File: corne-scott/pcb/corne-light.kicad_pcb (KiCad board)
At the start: 2 copper layers, 271.8 x 105.6 mm, 118 parts, among them J1 MJ-4PP-9, J2 OLED, J5 Breakaway_Tabs, J6 MJ-4PP-9, J7 OLED, SW1 SW_PUSH, SW10 SW_PUSH, SW11 SW_PUSH, SW12 SW_PUSH, SW13 SW_PUSH, SW14 SW_PUSH, SW15 SW_PUSH, SW16 SW_PUSH, SW17 SW_PUSH, SW18 SW_PUSH, SW19 SW_PUSH, SW2 SW_PUSH, SW20 SW_PUSH, SW21 SW_PUSH, SW22 SW_PUSH, SW23 SW_PUSH, SW24 SW_PUSH, SW25 SW_PUSH, SW26 SW_PUSH, SW27 SW_PUSH, SW28 SW_PUSH, SW29 SW_PUSH, SW3 SW_PUSH, SW30 SW_PUSH, SW31 SW_PUSH, SW32 SW_PUSH, SW33 SW_PUSH, SW34 SW_PUSH, SW35 SW_PUSH, SW36 SW_PUSH, SW37 SW_PUSH, SW38 SW_PUSH, SW39 SW_PUSH, SW4 SW_PUSH, SW40 SW_PUSH, SW41 SW_PUSH, SW42 SW_PUSH, SW5 SW_PUSH, SW6 SW_PUSH, SW7 SW_PUSH, SW8 SW_PUSH, SW9 SW_PUSH, U1 ProMicro, U2 ProMicro

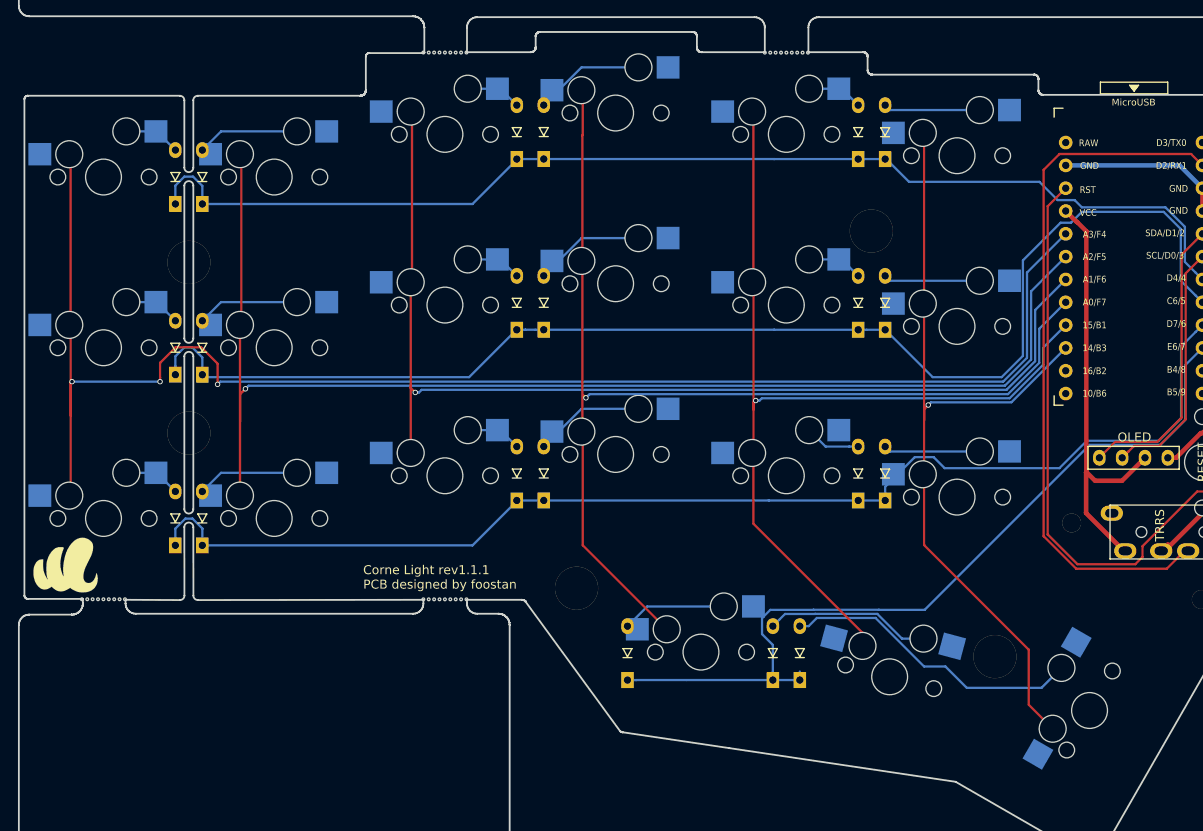
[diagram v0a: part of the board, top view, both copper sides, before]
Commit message: Rotate left side switches and diodes
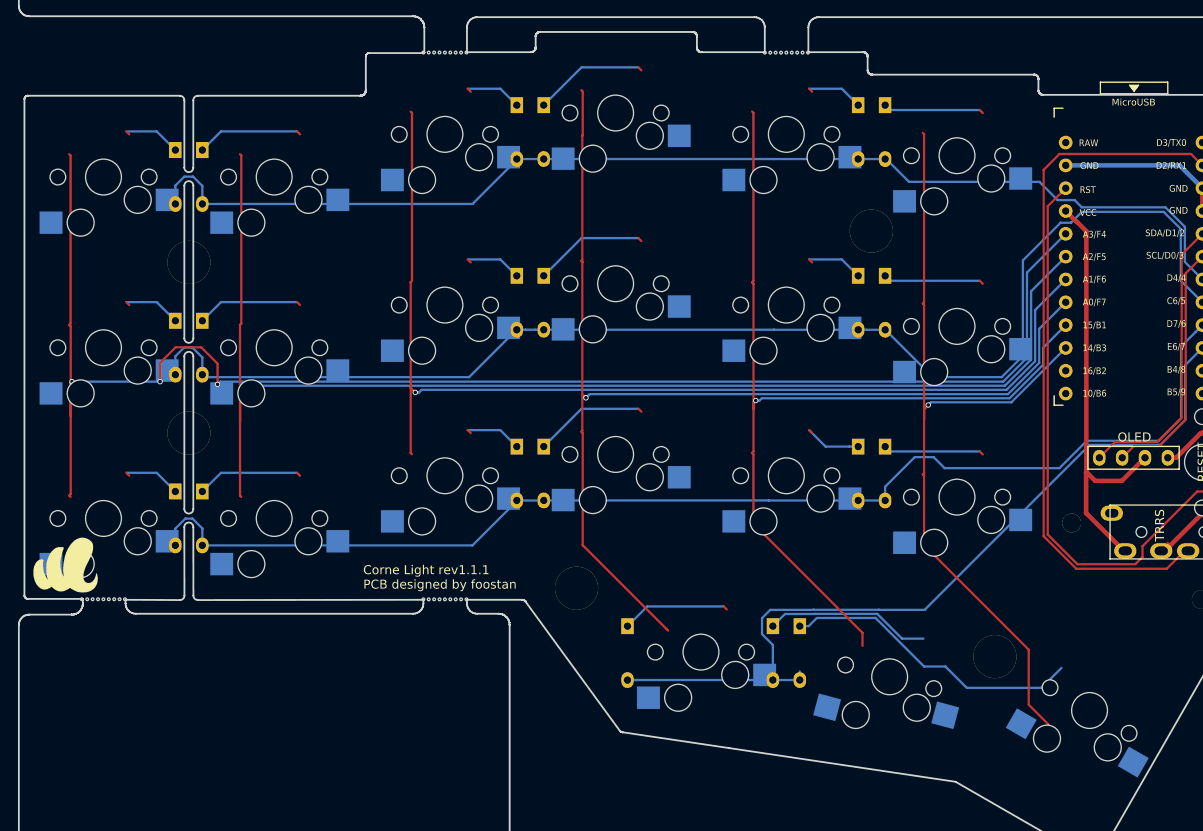
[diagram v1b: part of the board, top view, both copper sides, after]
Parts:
- D1, D10, D11, D12, D13, D14, D15, D16, D17, D18, D19, D2, D20, D21, D3, D4, D5, D6, D7, D8, D9: moved to B.Cu
- turned D1 to 270 degrees
- turned D10 to 270 degrees
- turned D11 to 270 degrees
- turned D12 to 270 degrees
- turned D13 to 270 degrees
- turned D14 to 270 degrees
- turned D15 to 270 degrees
- turned D16 to 270 degrees
- turned D17 to 270 degrees
- turned D18 to 270 degrees
- turned D19 to 270 degrees
- turned D2 to 270 degrees
- turned D20 to 270 degrees
- turned D21 to 270 degrees
- turned D3 to 270 degrees
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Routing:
- net row3: track 92.6 -> 156.3 mm
- net row2: track 135.8 -> 189.0 mm
- net row1: track 145.0 -> 198.2 mm
- net row0: track 129.2 -> 182.4 mm
- net Net-(D21-Pad2): track 33.6 -> 0.00 mm
- net Net-(D20-Pad2): track 18.5 -> 0.00 mm
- net Net-(D16-Pad2): track 12.3 -> 0.00 mm
- net Net-(D4-Pad2): track 12.3 -> 0.00 mm
- net Net-(D10-Pad2): track 12.3 -> 0.00 mm
- net Net-(D19-Pad2): track 11.6 -> 0.00 mm
- net Net-(D8-Pad2): track 11.4 -> 0.00 mm
- net Net-(D2-Pad2): track 11.4 -> 0.00 mm
- net Net-(D14-Pad2): track 11.4 -> 0.00 mm
- net Net-(D6-Pad2): track 10.8 -> 0.00 mm
- net Net-(D18-Pad2): track 10.8 -> 0.00 mm
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
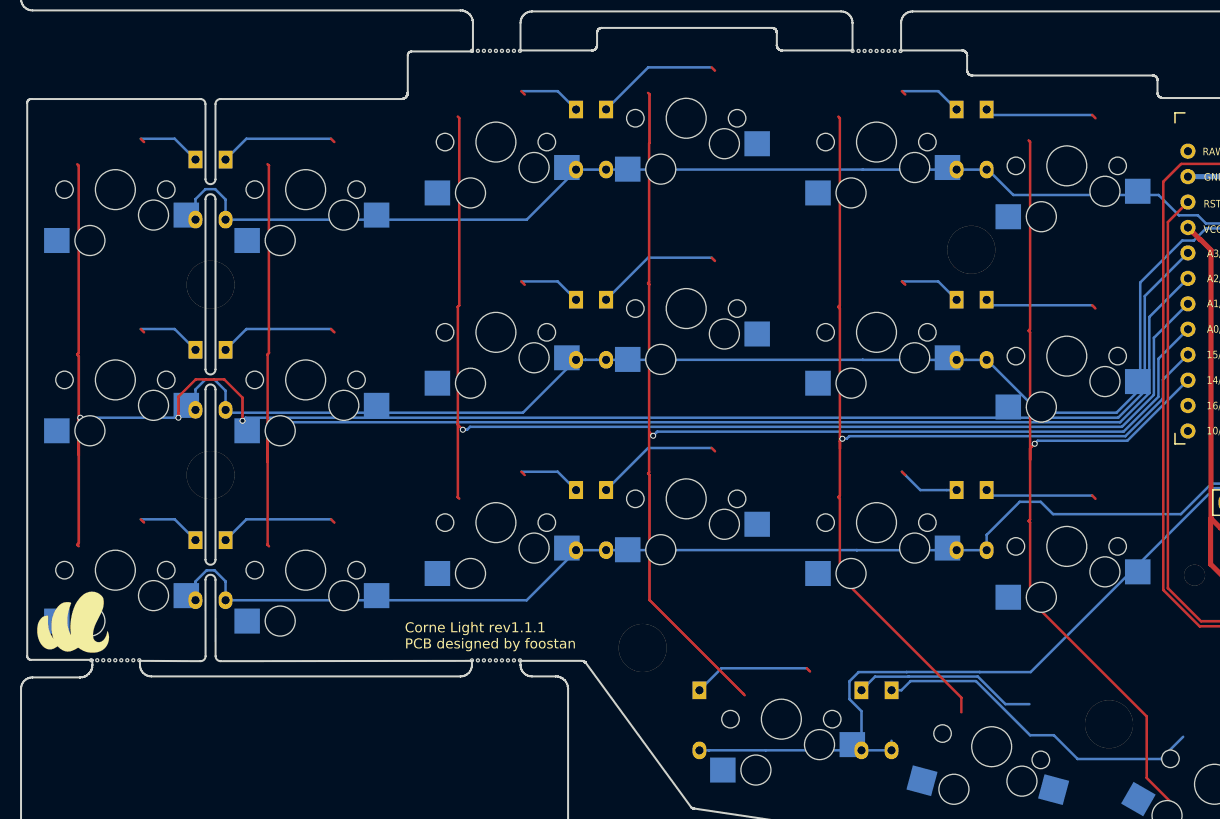
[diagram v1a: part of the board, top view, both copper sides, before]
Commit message: Adjust left side diodes
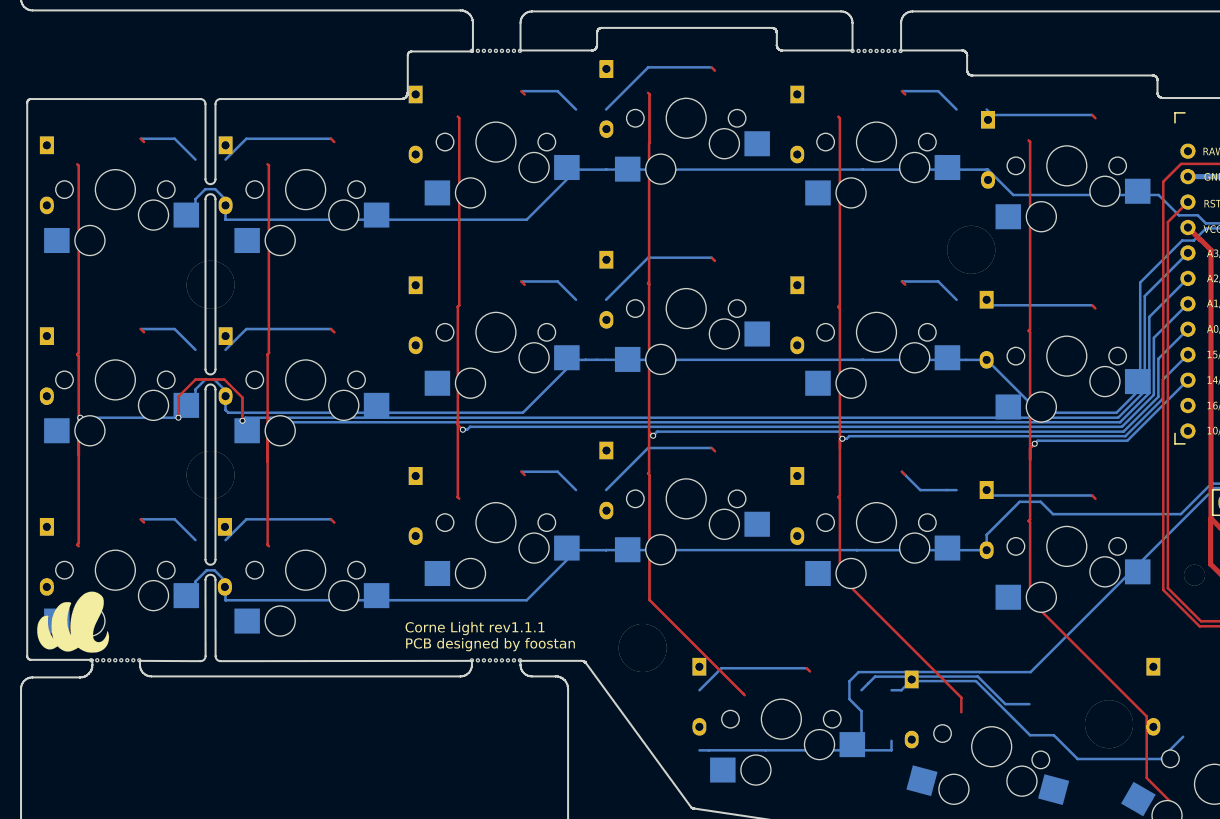
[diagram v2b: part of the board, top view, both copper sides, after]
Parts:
- moved D21 26.3 mm to (125.8, 96.6)
- moved D3 16.1 mm to (52.2, 39.4)
- moved D9 16.1 mm to (52.2, 58.5)
- moved D15 16.1 mm to (52.2, 77.5)
- moved D5 16.0 mm to (90.3, 39.4)
- moved D11 16.0 mm to (90.3, 58.5)
- moved D17 16.0 mm to (90.3, 77.5)
- moved D1 14.9 mm to (15.3, 44.5)
- moved D7 14.9 mm to (15.3, 63.5)
- moved D13 14.9 mm to (15.3, 82.6)
- moved D20 5.13 mm to (101.7, 97.8)
- moved D4 4.04 mm to (71.2, 36.9)
- moved D10 3.99 mm to (71.2, 55.9)
- moved D16 3.94 mm to (71.2, 75.0)
- moved D19 2.35 mm to (80.5, 96.6)
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
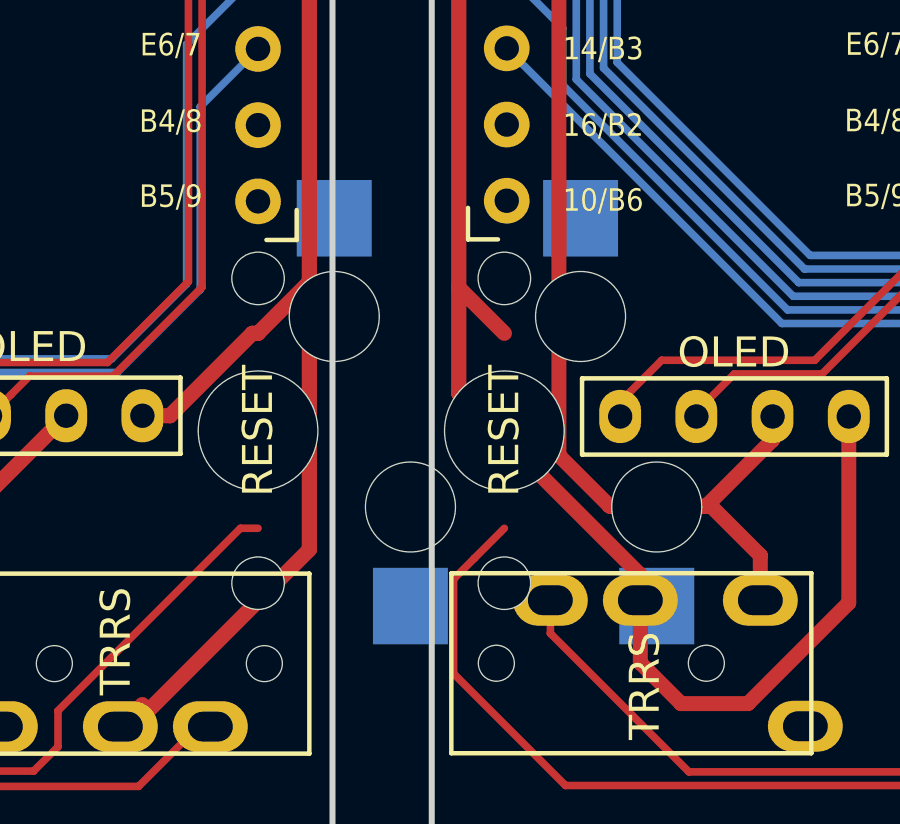
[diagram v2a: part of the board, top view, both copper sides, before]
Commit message: Add back reset switches I accidentally turned into mx switches
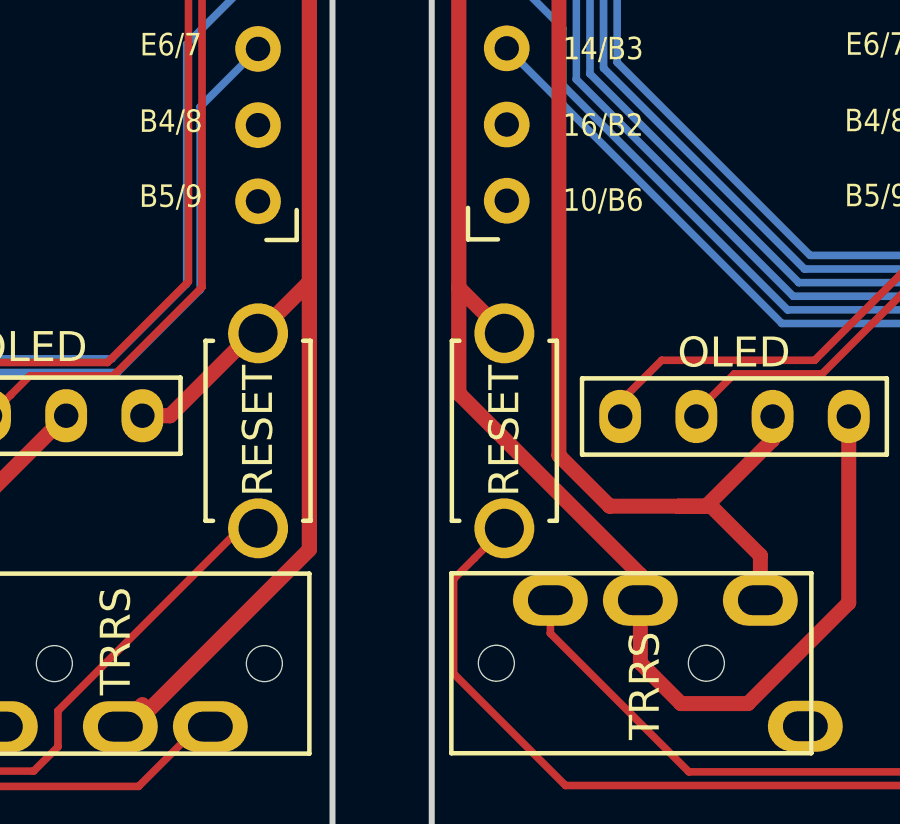
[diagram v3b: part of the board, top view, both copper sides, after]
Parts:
- RSW1, RSW2: footprint MX_Only:MXOnly-1U-Hotswap -> kbd:ResetSW_1side
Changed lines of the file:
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@@
     (add_net row3_r)
+  )
+  (module kbd:ResetSW_1side (layer F.Cu)
+    (at 152.7145 77.671 270)
+    (fp_text reference RSW2 (at 0 2.55 90) (layer F.SilkS) hide
+      (effects (font (size 1 1) (thickness 0.15)))
+    )
+    (fp_text value SW_PUSH (at 0 -2.55 90) (layer F.Fab)
+      (effects (font (size 1 1) (thickness 0.15)))
+    )
+    (fp_text user RESET (at 0 0 90) (layer F.SilkS)
+      (effects (font (size 1 1) (thickness 0.15)))
+    )
+    (fp_line (start 3 -1.75) (end 3 -1.5) (layer F.SilkS) (width 0.15))
+    (fp_line (start -3 -1.75) (end 3 -1.75) (layer F.SilkS) (width 0.15))
+    (fp_line (start -3 -1.75) (end -3 -1.5) (layer F.SilkS) (width 0.15))
+    (fp_line (start -3 1.75) (end -3 1.5) (layer F.SilkS) (width 0.15))
+    (fp_line (start 3 1.75) (end 3 1.5) (layer F.SilkS) (width 0.15))
+    (fp_line (start -3 1.75) (end 3 1.75) (layer F.SilkS) (width 0.15))
+    (fp_text user %R (at 0 3.048 90) (layer B.SilkS)
+      (effects (font (size 1 1) (thickness 0.15)) (justify mirror))
+    )
+    (pad 2 thru_hole circle (at -3.25 0 270) (size 2 2) (drill 1.3) (layers *.Cu F.SilkS B.Mask)
+      (net 88 GNDA))
+    (pad 1 thru_hole circle (at 3.25 0 270) (size 2 2) (drill 1.3) (layers *.Cu F.SilkS B.Mask)
+      (net 75 reset_r))
+  )
+  (module kbd:ResetSW_1side (layer F.Cu)
+    (at 144.5045 77.671 270)
+    (fp_text reference RSW1 (at 0 2.55 270) (layer F.SilkS) hide
+      (effects (font (size 1 1) (thickness 0.15)))
+    )
+    (fp_text value SW_PUSH (at 0 -2.55 270) (layer F.Fab)
+      (effects (font (size 1 1) (thickness 0.15)))
+    )
+    (fp_text user RESET (at 0 0 270) (layer F.SilkS)
+      (effects (font (size 1 1) (thickness 0.15)))
+    )
+    (fp_line (start 3 -1.75) (end 3 -1.5) (layer F.SilkS) (width 0.15))
+    (fp_line (start -3 -1.75) (end 3 -1.75) (layer F.SilkS) (width 0.15))
+    (fp_line (start -3 -1.75) (end -3 -1.5) (layer F.SilkS) (width 0.15))
+    (fp_line (start -3 1.75) (end -3 1.5) (layer F.SilkS) (width 0.15))
+    (fp_line (start 3 1.75) (end 3 1.5) (layer F.SilkS) (width 0.15))
+    (fp_line (start -3 1.75) (end 3 1.75) (layer F.SilkS) (width 0.15))
+    (fp_text user %R (at 0 3.048 90) (layer B.SilkS)
+      (effects (font (size 1 1) (thickness 0.15)) (justify mirror))
+    )
+    (pad 2 thru_hole circle (at -3.25 0 270) (size 2 2) (drill 1.3) (layers *.Cu F.SilkS B.Mask)
+      (net 26 GND))
+    (pad 1 thru_hole circle (at 3.25 0 270) (size 2 2) (drill 1.3) (layers *.Cu F.SilkS B.Mask)
+      (net 36 reset))
   )
   (module MX_Only:MXOnly-1U-Hotswap (layer F.Cu)
@@
     (pad "" np_thru_hole circle (at 2.54 -5.08 180) (size 3 3) (drill 3) (layers *.Cu *.Mask))
   )
-  (module MX_Only:MXOnly-1U-Hotswap (layer F.Cu)
-    (at 152.7145 77.671 270)
-    (attr smd)
-    (fp_text reference RSW2 (at 0 2.55 90) (layer F.SilkS) hide
-      (effects (font (size 1 1) (thickness 0.15)))
-    )
-    (fp_text value SW_PUSH (at 0 -2.55 90) (layer F.Fab)
-      (effects (font (size 1 1) (thickness 0.15)))
-    )
-    (fp_line (start -5.842 -1.27) (end -5.842 -3.81) (layer B.CrtYd) (width 0.15))
-    (fp_line (start -8.382 -1.27) (end -5.842 -1.27) (layer B.CrtYd) (width 0.15))
-    (fp_line (start -8.382 -3.81) (end -8.382 -1.27) (layer B.CrtYd) (width 0.15))
-    (fp_line (start -5.842 -3.81) (end -8.382 -3.81) (layer B.CrtYd) (width 0.15))
-    (fp_line (start 4.572 -3.81) (end 4.572 -6.35) (layer B.CrtYd) (width 0.15))
-    (fp_line (start 7.112 -3.81) (end 4.572 -3.81) (layer B.CrtYd) (width 0.15))
-    (fp_line (start 7.112 -6.35) (end 7.112 -3.81) (layer B.CrtYd) (width 0.15))
-    (fp_line (start 4.572 -6.35) (end 7.112 -6.35) (layer B.CrtYd) (width 0.15))
-    (fp_circle (center -3.81 -2.54) (end -3.81 -4.064) (layer B.CrtYd) (width 0.15))
-    (fp_circle (center 2.54 -5.08) (end 2.54 -6.604) (layer B.CrtYd) (width 0.15))
-    (fp_text user %R (at 0 3.048 90) (layer B.SilkS)
-      (effects (font (size 1 1) (thickness 0.15)) (justify mirror))
-    )
-    (fp_line (start -9.525 9.525) (end -9.525 -9.525) (layer Dwgs.User) (width 0.15))
-    (fp_line (start 9.525 9.525) (end -9.525 9.525) (layer Dwgs.User) (width 0.15))
-    (fp_line (start 9.525 -9.525) (end 9.525 9.525) (layer Dwgs.User) (width 0.15))
-    (fp_line (start -9.525 -9.525) (end 9.525 -9.525) (layer Dwgs.User) (width 0.15))
-    (fp_line (start -7 -7) (end -7 -5) (layer Dwgs.User) (width 0.15))
-    (fp_line (start -5 -7) (end -7 -7) (layer Dwgs.User) (width 0.15))
-    (fp_line (start -7 7) (end -5 7) (layer Dwgs.User) (width 0.15))
-    (fp_line (start -7 5) (end -7 7) (layer Dwgs.User) (width 0.15))
-    (fp_line (start 7 7) (end 7 5) (layer Dwgs.User) (width 0.15))
-    (fp_line (start 5 7) (end 7 7) (layer Dwgs.User) (width 0.15))
-    (fp_line (start 7 -7) (end 7 -5) (layer Dwgs.User) (width 0.15))
-    (fp_line (start 5 -7) (end 7 -7) (layer Dwgs.User) (width 0.15))
-    (fp_text user RESET (at 0 0 90) (layer F.SilkS)
-      (effects (font (size 1 1) (thickness 0.15)))
-    )
-    (pad 2 smd rect (at 5.842 -5.08 270) (size 2.55 2.5) (layers B.Cu B.Paste B.Mask)
-      (net 88 GNDA))
-    (pad 1 smd rect (at -7.085 -2.54 270) (size 2.55 2.5) (layers B.Cu B.Paste B.Mask)
-      (net 75 reset_r))
-    (pad "" np_thru_hole circle (at 5.08 0 318.0996) (size 1.75 1.75) (drill 1.75) (layers *.Cu *.Mask))
-    (pad "" np_thru_hole circle (at -5.08 0 318.0996) (size 1.75 1.75) (drill 1.75) (layers *.Cu *.Mask))
-    (pad "" np_thru_hole circle (at -3.81 -2.54 270) (size 3 3) (drill 3) (layers *.Cu *.Mask))
-    (pad "" np_thru_hole circle (at 0 0 270) (size 3.9878 3.9878) (drill 3.9878) (layers *.Cu *.Mask))
-    (pad "" np_thru_hole circle (at 2.54 -5.08 270) (size 3 3) (drill 3) (layers *.Cu *.Mask))
-  )
-  (module MX_Only:MXOnly-1U-Hotswap (layer F.Cu)
-    (at 144.5045 77.671 270)
-    (attr smd)
-    (fp_text reference RSW1 (at 0 2.55 270) (layer F.SilkS) hide
-      (effects (font (size 1 1) (thickness 0.15)))
-    )
-    (fp_text value SW_PUSH (at 0 -2.55 270) (layer F.Fab)
-      (effects (font (size 1 1) (thickness 0.15)))
-    )
-    (fp_line (start -5.842 -1.27) (end -5.842 -3.81) (layer B.CrtYd) (width 0.15))
-    (fp_line (start -8.382 -1.27) (end -5.842 -1.27) (layer B.CrtYd) (width 0.15))
-    (fp_line (start -8.382 -3.81) (end -8.382 -1.27) (layer B.CrtYd) (width 0.15))
-    (fp_line (start -5.842 -3.81) (end -8.382 -3.81) (layer B.CrtYd) (width 0.15))
-    (fp_line (start 4.572 -3.81) (end 4.572 -6.35) (layer B.CrtYd) (width 0.15))
-    (fp_line (start 7.112 -3.81) (end 4.572 -3.81) (layer B.CrtYd) (width 0.15))
-    (fp_line (start 7.112 -6.35) (end 7.112 -3.81) (layer B.CrtYd) (width 0.15))
-    (fp_line (start 4.572 -6.35) (end 7.112 -6.35) (layer B.CrtYd) (width 0.15))
-    (fp_circle (center -3.81 -2.54) (end -3.81 -4.064) (layer B.CrtYd) (width 0.15))
-    (fp_circle (center 2.54 -5.08) (end 2.54 -6.604) (layer B.CrtYd) (width 0.15))
-    (fp_text user %R (at 0 3.048 90) (layer B.SilkS)
-      (effects (font (size 1 1) (thickness 0.15)) (justify mirror))
-    )
-    (fp_line (start -9.525 9.525) (end -9.525 -9.525) (layer Dwgs.User) (width 0.15))
-    (fp_line (start 9.525 9.525) (end -9.525 9.525) (layer Dwgs.User) (width 0.15))
-    (fp_line (start 9.525 -9.525) (end 9.525 9.525) (layer Dwgs.User) (width 0.15))
-    (fp_line (start -9.525 -9.525) (end 9.525 -9.525) (layer Dwgs.User) (width 0.15))
-    (fp_line (start -7 -7) (end -7 -5) (layer Dwgs.User) (width 0.15))
-    (fp_line (start -5 -7) (end -7 -7) (layer Dwgs.User) (width 0.15))
-    (fp_line (start -7 7) (end -5 7) (layer Dwgs.User) (width 0.15))
-    (fp_line (start -7 5) (end -7 7) (layer Dwgs.User) (width 0.15))
-    (fp_line (start 7 7) (end 7 5) (layer Dwgs.User) (width 0.15))
-    (fp_line (start 5 7) (end 7 7) (layer Dwgs.User) (width 0.15))
-    (fp_line (start 7 -7) (end 7 -5) (layer Dwgs.User) (width 0.15))
-    (fp_line (start 5 -7) (end 7 -7) (layer Dwgs.User) (width 0.15))
-    (fp_text user RESET (at 0 0 270) (layer F.SilkS)
-      (effects (font (size 1 1) (thickness 0.15)))
-    )
-    (pad 2 smd rect (at 5.842 -5.08 270) (size 2.55 2.5) (layers B.Cu B.Paste B.Mask)
-      (net 26 GND))
-    (pad 1 smd rect (at -7.085 -2.54 270) (size 2.55 2.5) (layers B.Cu B.Paste B.Mask)
-      (net 36 reset))
-    (pad "" np_thru_hole circle (at 5.08 0 318.0996) (size 1.75 1.75) (drill 1.75) (layers *.Cu *.Mask))
-    (pad "" np_thru_hole circle (at -5.08 0 318.0996) (size 1.75 1.75) (drill 1.75) (layers *.Cu *.Mask))
-    (pad "" np_thru_hole circle (at -3.81 -2.54 270) (size 3 3) (drill 3) (layers *.Cu *.Mask))
-    (pad "" np_thru_hole circle (at 0 0 270) (size 3.9878 3.9878) (drill 3.9878) (layers *.Cu *.Mask))
-    (pad "" np_thru_hole circle (at 2.54 -5.08 270) (size 3 3) (drill 3) (layers *.Cu *.Mask))
-  )
   (module kbd:D3_TH (layer F.Cu)
